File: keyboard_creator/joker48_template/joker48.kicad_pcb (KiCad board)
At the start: 2 copper layers, 80 x 60 mm, 20 parts, among them U1 BL24C256A-SFRC, U2 STM32F411CEU6, X1 ARM JTAG, Y1 7325-0800A2010-00

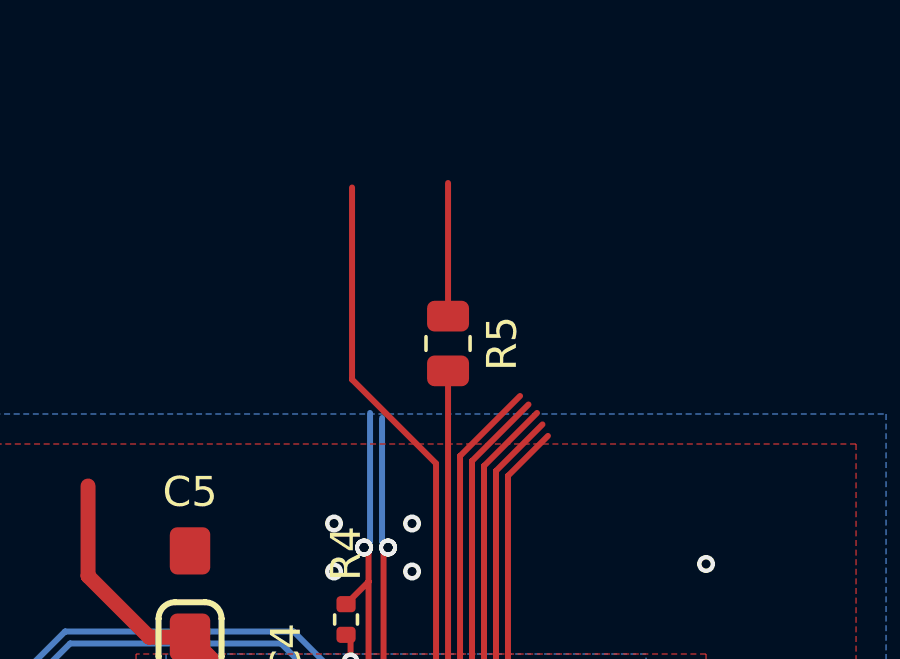
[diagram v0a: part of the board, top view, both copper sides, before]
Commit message: Update J48 metadata
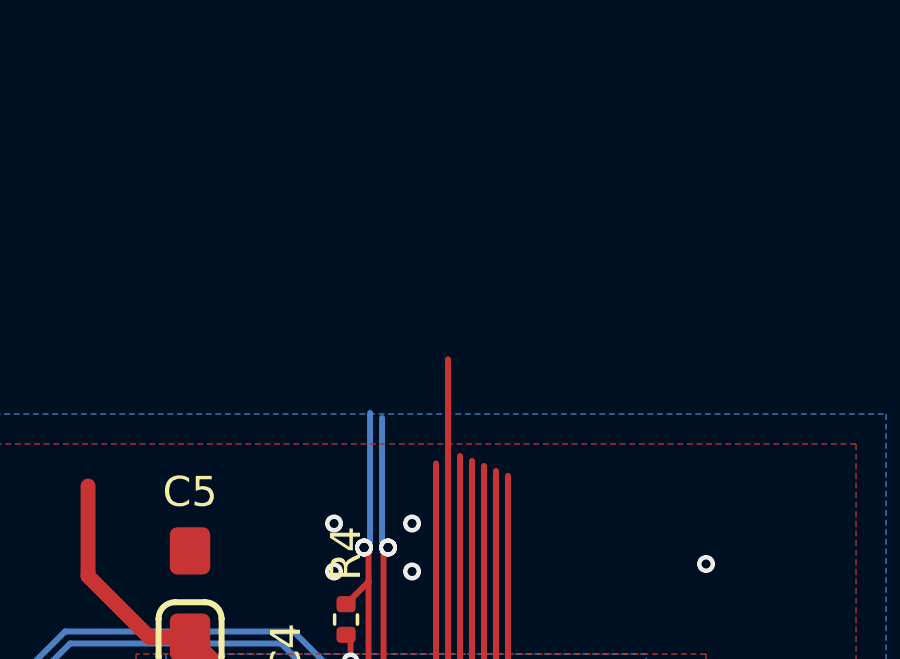
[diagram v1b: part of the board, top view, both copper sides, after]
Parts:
- removed R5: 0R, Resistor_SMD:R_0805_2012Metric
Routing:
- net unconnected-(U2-Pad31): track 21.2 -> 10.9 mm
- net 5V: track 4.42 -> 0.00 mm
- net unconnected-(U2-Pad29): track 13.9 -> 11.0 mm
- net RGB_3V3: track 13.5 -> 10.8 mm
- net unconnected-(U2-Pad27): track 13.1 -> 10.6 mm
- net unconnected-(U2-Pad26): track 12.6 -> 10.4 mm
- net unconnected-(U2-Pad25): track 12.1 -> 10.2 mm

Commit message: Typo fix
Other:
- board text added: "The files generated are compatible with KiCAD v6.0.1-2 version."
- board text added: "These files should also be accompanied of a libraries folder where the used libraries are added as submodules which last commit should point to the remote's HEAD."
- board text removed: "The files generated are compatible with KiCAD developmental ({dblquote}nightly{dblquote}) versions up to sptember 9, 2021 version."
- board text removed: "These files should also be accompanied of a librires folder where the used libraries are added as submodules which last commit should point to the remote's HEAD."
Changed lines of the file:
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@@
     (effects (font (size 0.8 0.8) (thickness 0.16)) (justify left))
   )
-  (gr_text "These files should also be accompanied of a librires folder where the used libraries are added as submodules which last commit should point to the remote's HEAD." (at 434.749972 21.649999) (layer "Cmts.User")
+  (gr_text "These files should also be accompanied of a libraries folder where the used libraries are added as submodules which last commit should point to the remote's HEAD." (at 434.749972 21.649999) (layer "Cmts.User")
     (effects (font (size 1 1) (thickness 0.2)) (justify left))
   )
@@
     (effects (font (size 1 1) (thickness 0.25)) (justify left))
   )
-  (gr_text "The files generated are compatible with KiCAD developmental ({dblquote}nightly{dblquote}) versions up to sptember 9, 2021 version." (at 434.749972 18.649999) (layer "Cmts.User")
+  (gr_text "The files generated are compatible with KiCAD v6.0.1-2 version." (at 434.749972 18.649999) (layer "Cmts.User")
     (effects (font (size 1 1) (thickness 0.2)) (justify left))
   )
